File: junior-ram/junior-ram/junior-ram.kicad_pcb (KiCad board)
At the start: 2 copper layers, 160 x 100 mm, 7 parts, among them IC1 74LS241, IC2 74LS241, IC3 74LS243, IC4 74LS243, IC5 GAL16V8, J1 C64AC

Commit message: junior ram
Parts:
- removed REF**: EuroBoard160mmX100mm, EuroBoard_Outline:EuroBoard160mmX100mm
- added IC6: 62256, elektor:DIL-28, F.Cu at (130.8, 67.3)
- added IC7: 62256, elektor:DIL-28, F.Cu at (130.8, 90.2)
- added IC8: 27C256, elektor:DIL-28, F.Cu at (130.8, 113.0)
- added IC9: 27C256, elektor:DIL-28, F.Cu at (130.8, 135.9)
- added J2: Conn_01x03_Male, elektor:CONN-3, F.Cu at (149.9, 118.1)
- added J3: Conn_01x03_Male, elektor:CONN-3, F.Cu at (149.9, 141.0)
- moved IC4 13.1 mm to (85.1, 71.1), turned to 270 degrees
- moved IC3 7.73 mm to (99.1, 71.1), turned to 270 degrees
- moved IC2 5.39 mm to (85.1, 97.8)
- moved IC1 4.58 mm to (85.1, 129.5)
- moved IC5 4.58 mm to (99.1, 97.8)
- moved J1 4.02 mm to (68.6, 61.0)
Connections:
- IC5 pad 1: AB11 -> AB14
- IC5 pad 2: AB12 -> AB15
- IC5 pad 3: AB13 -> AB12
- IC5 pad 4: AB14 -> AB13
- IC5 pad 5: AB15 -> AB11
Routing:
- net +5V: track 0.00 -> 344.0 mm
- net GND: track 0.00 -> 201.9 mm
- net AB14: track 0.00 -> 156.9 mm, vias 0 -> 1
- net AB12: track 0.00 -> 134.3 mm, vias 0 -> 1
- net AB8: track 0.00 -> 131.3 mm, vias 0 -> 1
- net AB6: track 0.00 -> 126.9 mm, vias 0 -> 1
- net AB4: track 0.00 -> 125.9 mm
- net AB7: track 0.00 -> 125.6 mm
- net AB13: track 0.00 -> 124.6 mm, vias 0 -> 1
- net AB2: track 0.00 -> 123.1 mm, vias 0 -> 1
- net AB10: track 0.00 -> 122.2 mm, vias 0 -> 1
- net AB9: track 0.00 -> 121.7 mm, vias 0 -> 1
- net AB5: track 0.00 -> 121.6 mm
- net AB11: track 0.00 -> 120.1 mm, vias 0 -> 1
- net AB1: track 0.00 -> 119.8 mm, vias 0 -> 1
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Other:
- board size 160 x 100 mm -> 100 x 100 mm

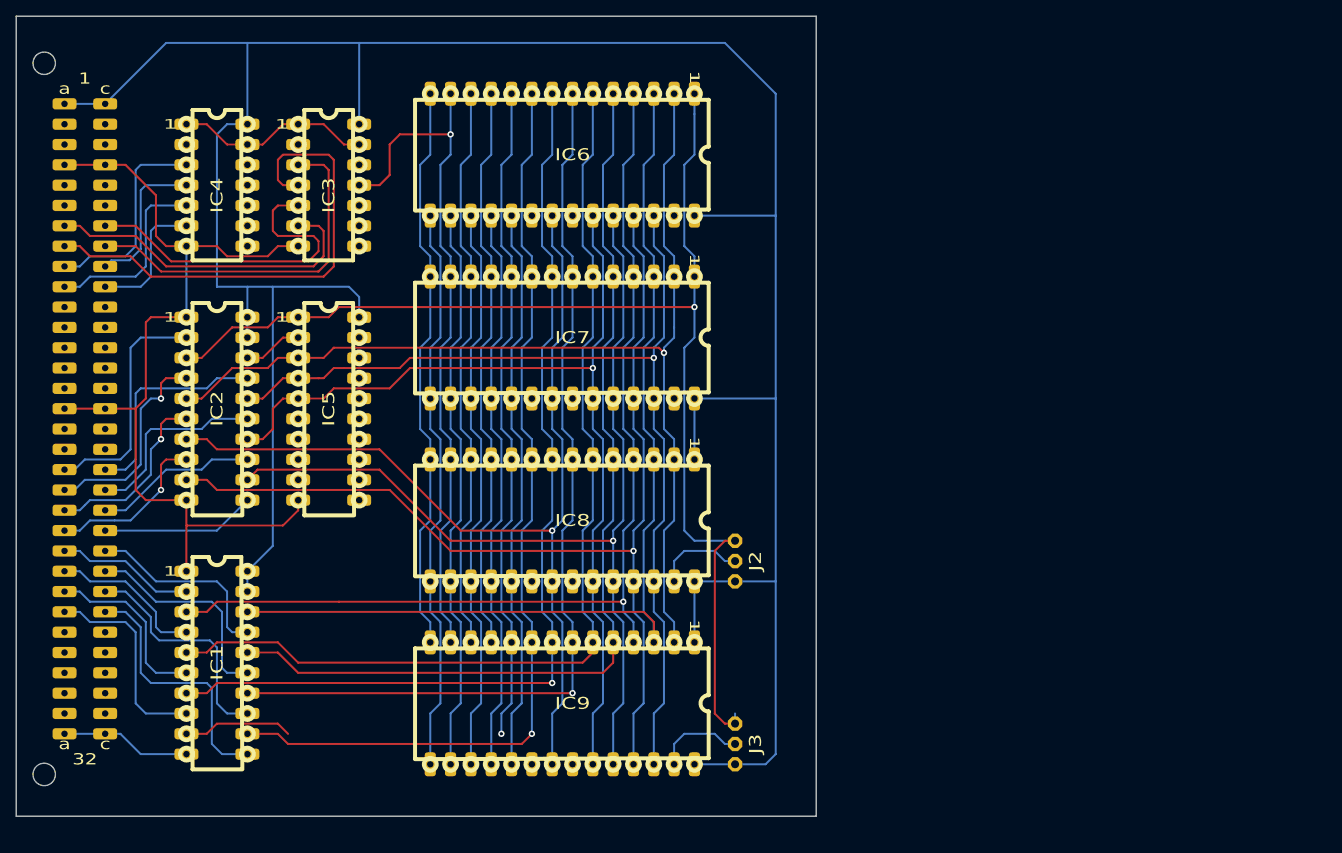
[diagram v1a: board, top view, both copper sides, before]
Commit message: junior ram routage complet
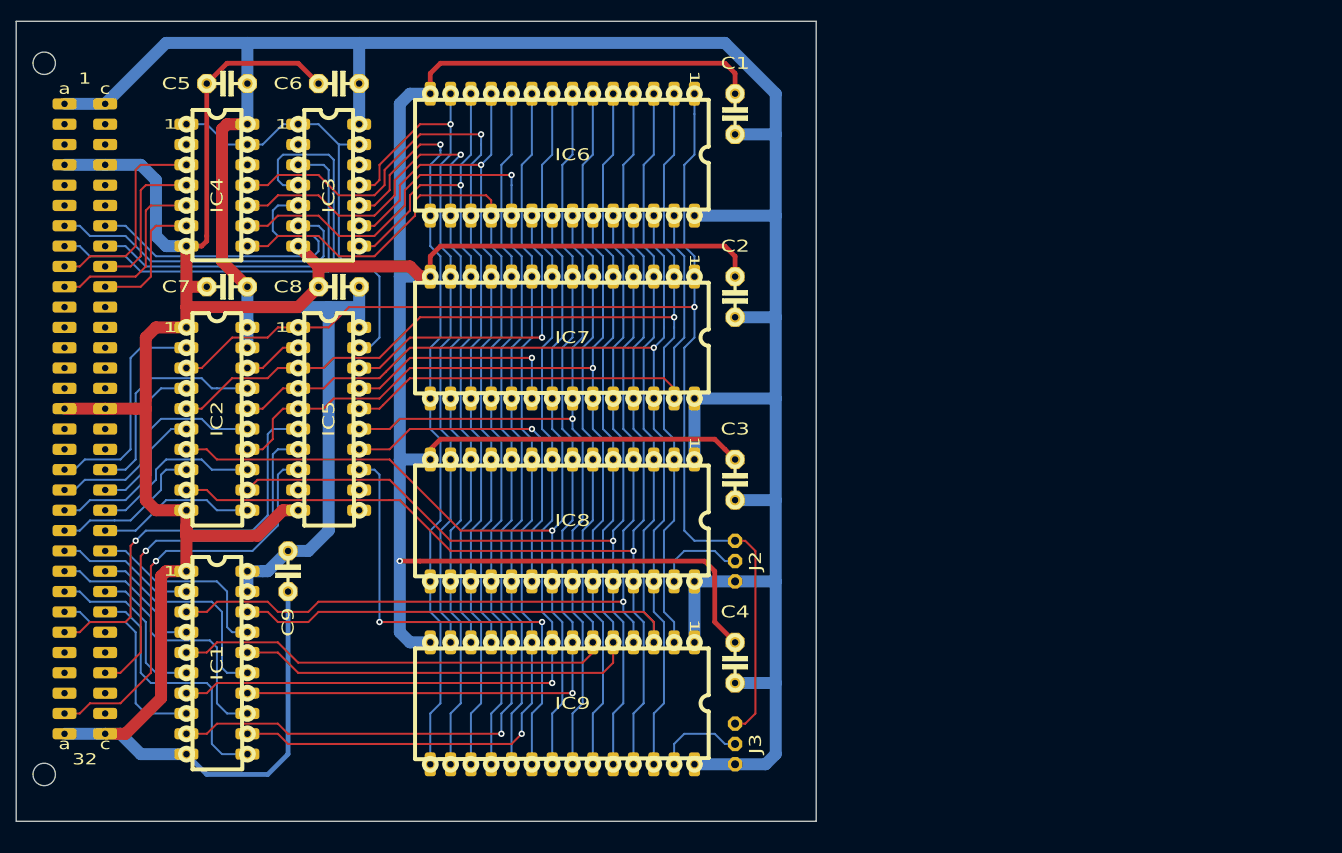
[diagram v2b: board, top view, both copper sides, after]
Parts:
- added C1: 100n, elektor:CAP-2-HEX, F.Cu at (149.9, 62.2)
- added C2: 100n, elektor:CAP-2-HEX, F.Cu at (149.9, 85.1)
- added C3: 100n, elektor:CAP-2-HEX, F.Cu at (149.9, 108.0)
- added C4: 100n, elektor:CAP-2-HEX, F.Cu at (149.9, 130.8)
- added C5: 100n, elektor:CAP-2-HEX, F.Cu at (86.4, 58.4)
- added C6: 100n, elektor:CAP-2-HEX, F.Cu at (100.3, 58.4)
- added C7: 100n, elektor:CAP-2-HEX, F.Cu at (86.4, 83.8)
- added C8: 100n, elektor:CAP-2-HEX, F.Cu at (100.3, 83.8)
- added C9: 100n, elektor:CAP-2-HEX, F.Cu at (94.0, 119.4)
- moved IC2 1.27 mm to (85.1, 99.1)
- moved IC5 1.27 mm to (99.1, 99.1)
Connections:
- IC5 pad 13: Net-(IC5-Pad13) -> ROM.CS2
- IC5 pad 14: Net-(IC5-Pad14) -> ROM.CS1
- IC5 pad 15: Net-(IC5-Pad15) -> OE
- IC5 pad 16: Net-(IC5-Pad16) -> WE
- IC5 pad 17: Net-(IC5-Pad17) -> RAM.CS2
- IC5 pad 18: Net-(IC5-Pad18) -> RAM.CS1
- IC5 pad 6: RAM.RW -> PHI2
- IC5 pad 7: Net-(IC5-Pad7) -> RW
- IC5 pad 8: Net-(IC5-Pad8) -> RAM.RW
- IC6 pad 20: Net-(IC6-Pad20) -> RAM.CS1
- IC6 pad 22: Net-(IC6-Pad22) -> OE
- IC6 pad 27: Net-(IC6-Pad27) -> WE
- IC7 pad 20: Net-(IC7-Pad20) -> RAM.CS2
- IC7 pad 22: Net-(IC7-Pad22) -> OE
- IC7 pad 27: Net-(IC7-Pad27) -> WE
- IC8 pad 20: Net-(IC8-Pad20) -> ROM.CS1
- IC8 pad 22: Net-(IC8-Pad22) -> OE
- IC9 pad 20: Net-(IC9-Pad20) -> ROM.CS2
- IC9 pad 22: Net-(IC9-Pad22) -> OE
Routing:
- net GND: track 201.9 -> 521.9 mm, vias 0 -> 1
- net OE: track 0.00 -> 98.9 mm, vias 0 -> 1
- net WE: track 0.00 -> 66.7 mm
- net ROM.CS2: track 0.00 -> 59.8 mm, vias 0 -> 2
- net RAM.RW: track 0.00 -> 53.4 mm, vias 0 -> 1
- net PHI2: track 0.00 -> 50.9 mm, vias 0 -> 1
- net RW: track 0.00 -> 47.6 mm, vias 0 -> 1
- net DB5: track 71.7 -> 117.5 mm, vias 0 -> 1
- net DB7: track 71.7 -> 115.7 mm, vias 0 -> 1
- net ROM.CS1: track 0.00 -> 42.7 mm, vias 0 -> 1
- net DB4: track 71.7 -> 112.4 mm, vias 0 -> 1
- net RAM.CS1: track 0.00 -> 40.2 mm, vias 0 -> 1
- net DB6: track 71.7 -> 110.2 mm
- net D.DIR: track 24.7 -> 55.5 mm
- net RAM.CS2: track 0.00 -> 28.2 mm, vias 0 -> 1
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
